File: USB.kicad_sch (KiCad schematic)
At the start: 40 parts, among them J1 USB_C_Receptacle_USB2.0_14P, J6 USB_C_Receptacle_USB2.0_14P, J7 USB_C_Receptacle_USB2.0_14P, U14 NUP2202, U15 NUP2202, U7 93LCxxBxxOT, U8 FT2232HQ, Y1 12MHz

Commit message: Finished board. Added BOM
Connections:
- no-connect marks 16 -> 17
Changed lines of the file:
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@@
+	)
+	(no_connect
+		(at 262.89 148.59)
 	)
 	(no_connect

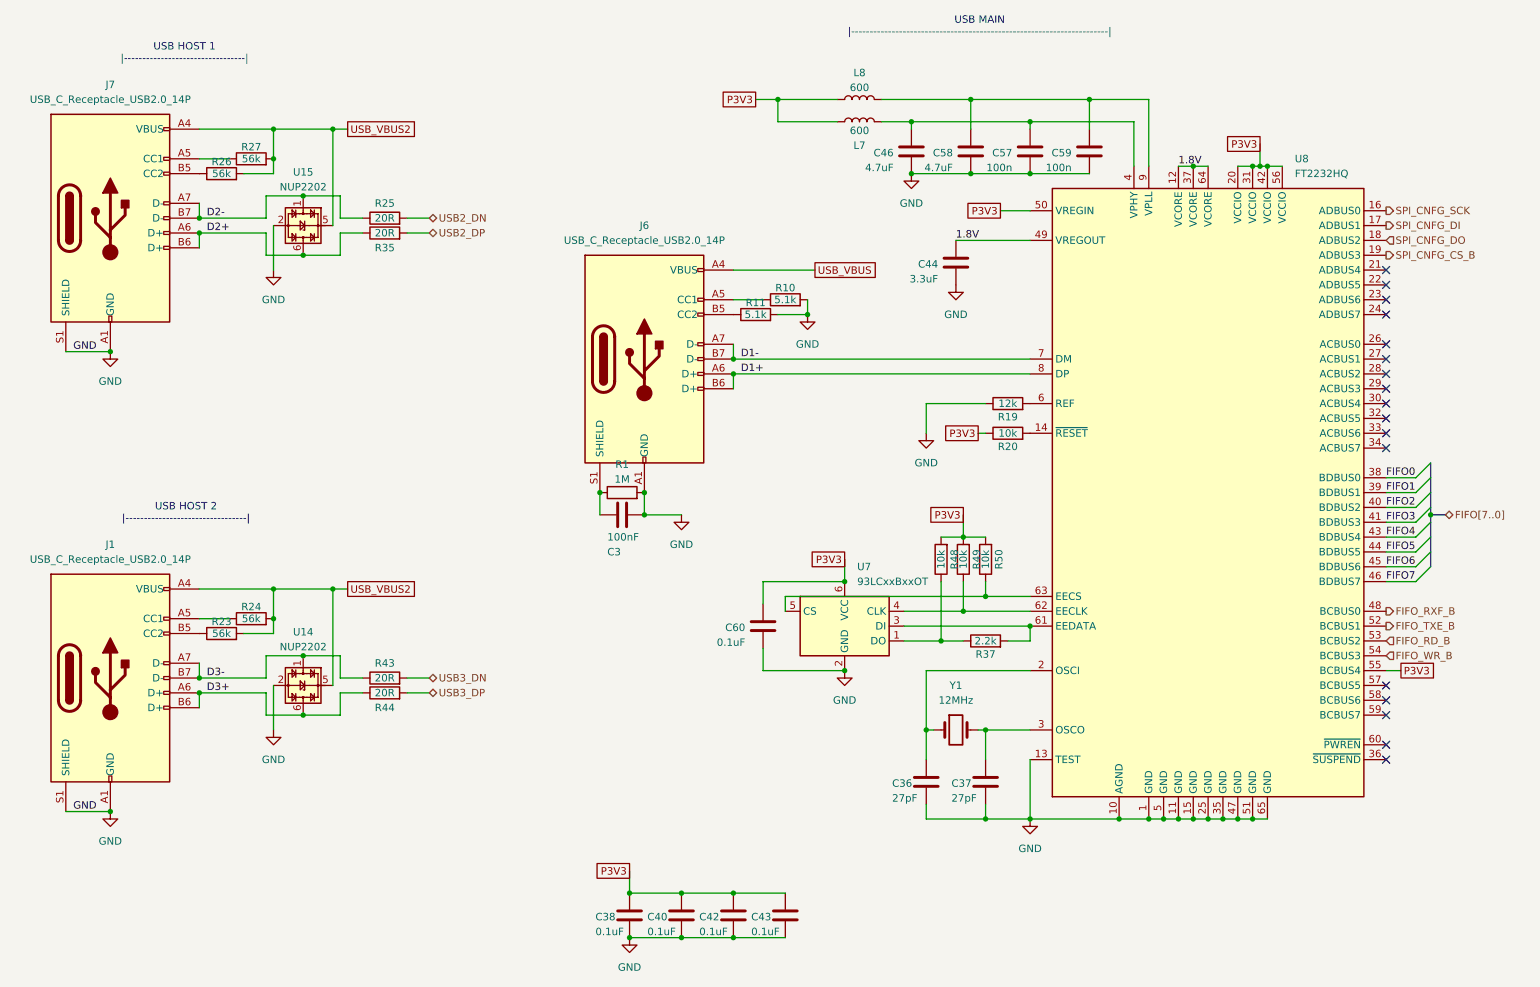
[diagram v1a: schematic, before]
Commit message: End of Version 1.0. Feedback received
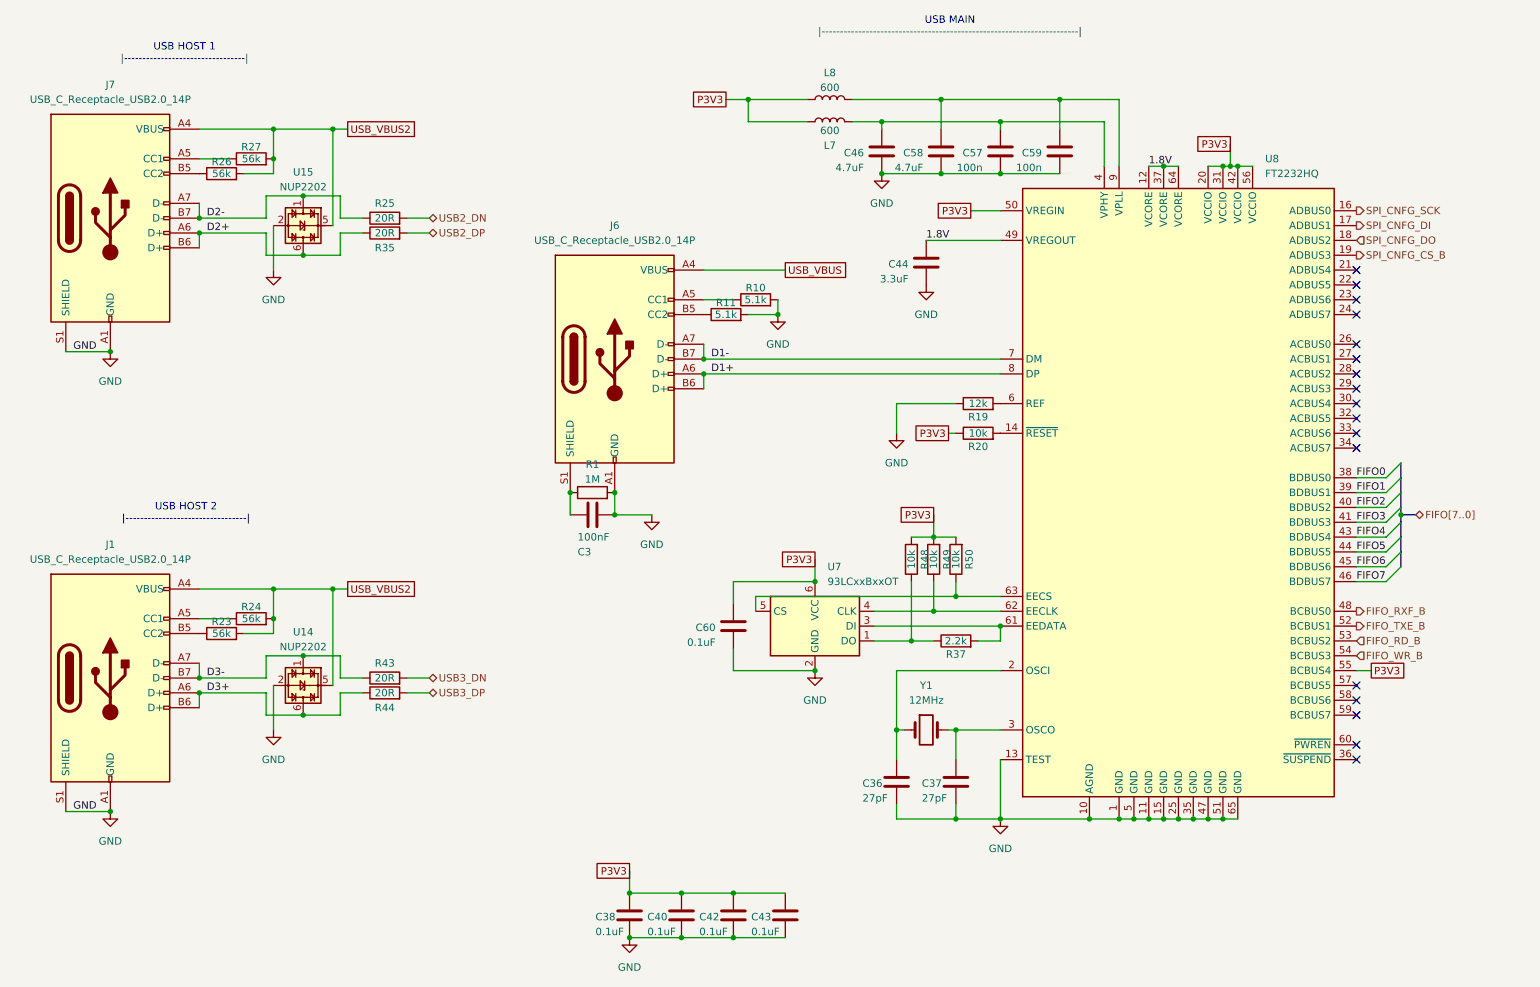
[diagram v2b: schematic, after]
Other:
- moved on the sheet: C3, C36, C37, C44, C46, C57, C58, C59, C60, J6, L7, L8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
